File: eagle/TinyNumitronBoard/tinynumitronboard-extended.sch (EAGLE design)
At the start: 25 parts

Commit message: Extended version : schema is ok but board is beta.
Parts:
- added LED3, LED4: (no value), led:LEDKA-3528ASYC
- added R17, R18, R19, R20, R21, R22, R23, R24, R25, R26, R27, R28, R29, R30, R31, R32: (no value), resistor:R-EU_0207/10
- added U$5, U$7: IV16TINY_NUMITRON, kalshagar:IV16TINY_NUMITRON
- added U$6, U$8: 74HC595_SMDDIP_COMBOTHINPAD, kalshagar:74HC595_SMDDIP_COMBOTHINPAD
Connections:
- new net N$39: R17.2, U$5.BOTTOMLEFT
- new net N$40: R18.2, U$5.BOTTOM
- new net N$41: R19.2, U$5.MIDDLE
- new net N$42: R20.2, U$5.TOPLEFT
- new net N$43: R21.2, U$5.TOP
- new net N$44: R22.2, U$5.BOTTOMRIGHT
- new net N$45: R23.2, U$5.TOPRIGHT
- new net N$46: R17.1, U$6.QA
- new net N$47: R18.1, U$6.QB
- new net N$48: R19.1, U$6.QC
- new net N$49: R20.1, U$6.QD
- new net N$50: R21.1, U$6.QE
- new net N$51: R22.1, U$6.QF
- new net N$52: R23.1, U$6.QG
- new net N$53: R24.1, U$6.QH
- new net N$54: LED3.A, R24.2, U$5.DOT
- new net N$62: R25.2, U$7.BOTTOMLEFT
- new net N$63: R26.2, U$7.BOTTOM
- new net N$64: R27.2, U$7.MIDDLE
- new net N$65: R28.2, U$7.TOPLEFT
- new net N$66: R29.2, U$7.TOP
- new net N$67: R30.2, U$7.BOTTOMRIGHT
- new net N$68: R31.2, U$7.TOPRIGHT
- new net N$69: R25.1, U$8.QA
- new net N$70: R26.1, U$8.QB
- new net N$71: R27.1, U$8.QC
- new net N$72: R28.1, U$8.QD
- new net N$73: R29.1, U$8.QE
- new net N$74: R30.1, U$8.QF
- new net N$75: R31.1, U$8.QG
- new net N$76: R32.1, U$8.QH
- new net N$77: LED4.A, R32.2, U$7.DOT
- new net N$78: U$4.SER
- net GND: now also LED3.C, LED4.C, U$4.G, U$4.GND
- net N$18: now also U$4.RCK
- net N$19: now also U$4.SCK
- net N$22: now also U$4.QH*
- net VCC: now also U$4.SCL, U$4.VCC, U$5.VCC, U$7.VCC
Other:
- moved on the sheet: JP_OUTPUT, LED2, R10, R11, R12, R13, R14, R15, R16, R9, U$4

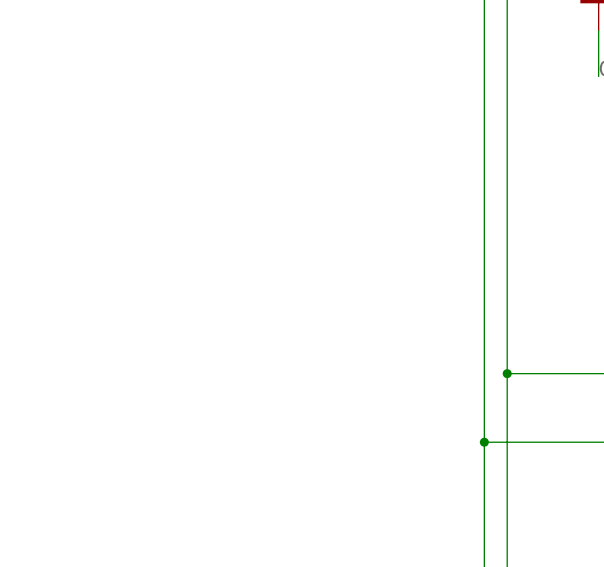
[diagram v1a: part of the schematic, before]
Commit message: added mounting holes and improved placement.
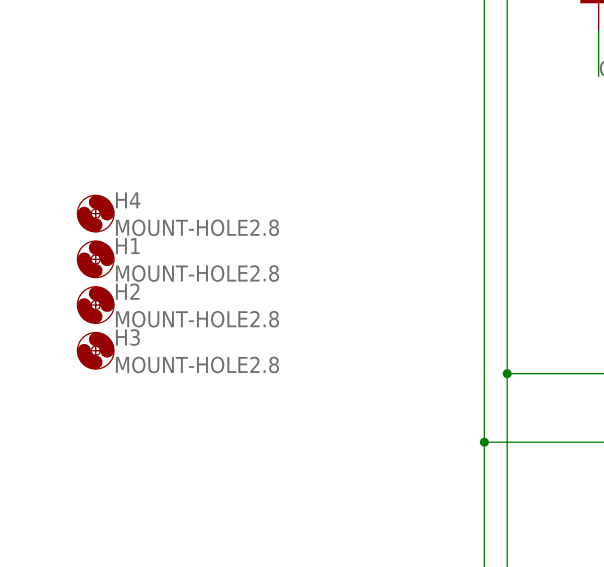
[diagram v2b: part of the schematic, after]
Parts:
- added H1, H2, H3, H4: MOUNT-HOLE2.8, holes:MOUNT-HOLE2.8
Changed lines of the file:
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@@
 <layer number="144" name="Drill_legend" color="7" fill="1" visible="no" active="yes"/>
 <layer number="151" name="HeatSink" color="7" fill="1" visible="no" active="yes"/>
+<layer number="199" name="Contour" color="7" fill="1" visible="yes" active="yes"/>
 <layer number="200" name="200bmp" color="1" fill="10" visible="no" active="yes"/>
 <layer number="201" name="201bmp" color="2" fill="10" visible="no" active="yes"/>
@@
 <part name="R32" library="resistor" deviceset="R-EU_" device="0207/10"/>
 <part name="U$8" library="kalshagar" deviceset="74HC595_SMDDIP_COMBO" device="THINPAD"/>
+<part name="H4" library="holes" deviceset="MOUNT-HOLE" device="2.8"/>
+<part name="H1" library="holes" deviceset="MOUNT-HOLE" device="2.8"/>
+<part name="H2" library="holes" deviceset="MOUNT-HOLE" device="2.8"/>
+<part name="H3" library="holes" deviceset="MOUNT-HOLE" device="2.8"/>
 </parts>
 <sheets>
@@
 <instance part="R32" gate="G$1" x="-17.78" y="-66.04"/>
 <instance part="U$8" gate="G$1" x="-48.26" y="-63.5"/>
+<instance part="H4" gate="G$1" x="-144.78" y="22.86"/>
+<instance part="H1" gate="G$1" x="-144.78" y="17.78"/>
+<instance part="H2" gate="G$1" x="-144.78" y="12.7"/>
+<instance part="H3" gate="G$1" x="-144.78" y="7.62"/>
 </instances>
 <busses>

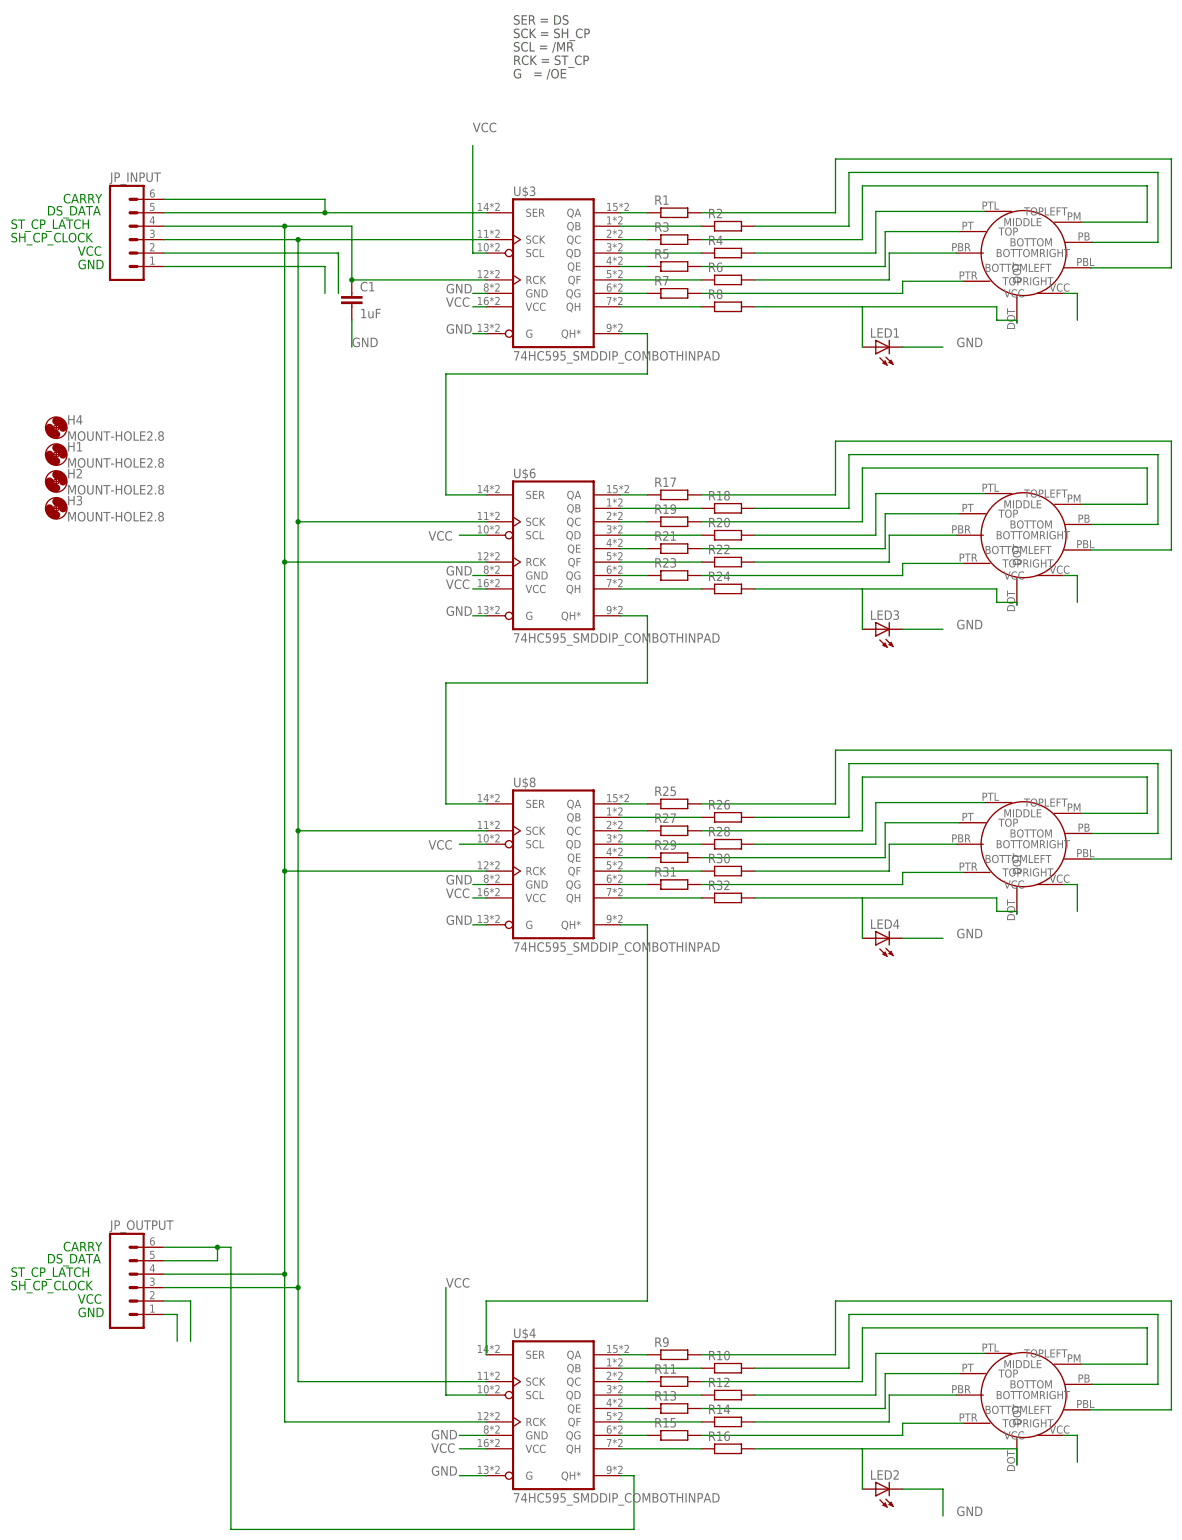
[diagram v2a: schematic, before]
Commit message: fixed the lots of missing wires ! all connections should be ok now.
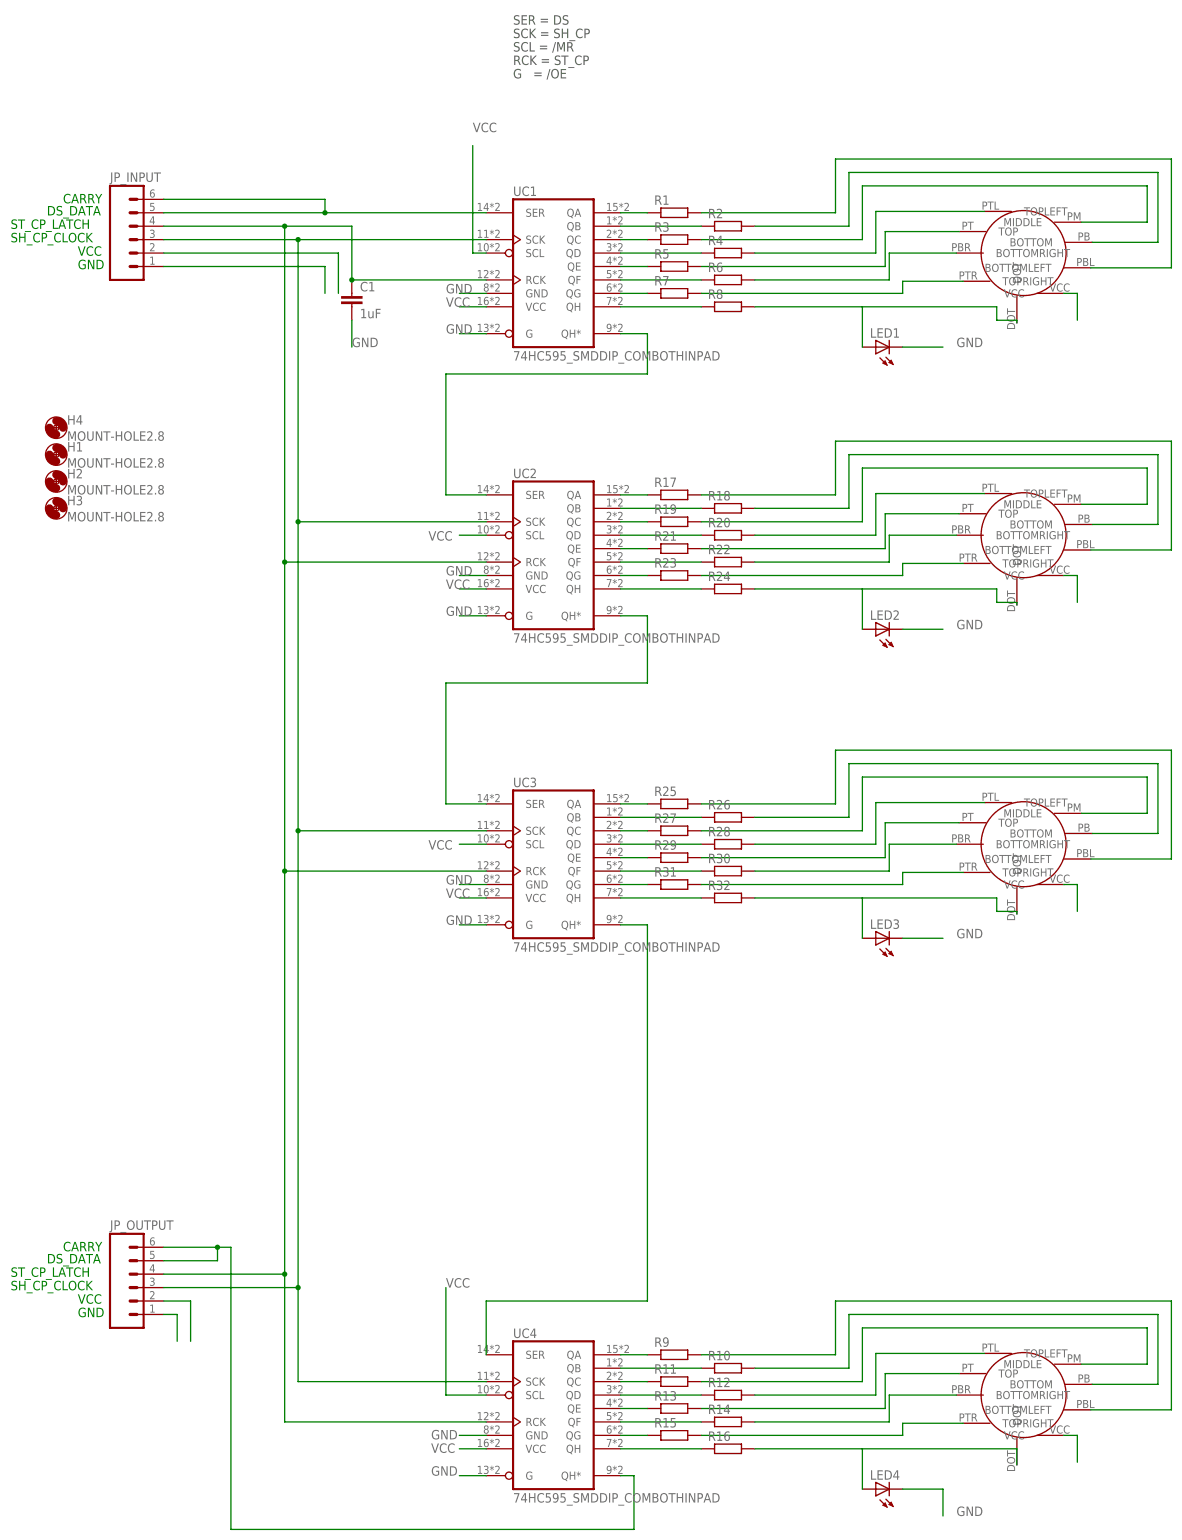
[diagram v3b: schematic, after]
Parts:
- renumbered U$3 to UC1, U$4 to UC4, U$6 to UC2, U$8 to UC3
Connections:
- removed net N$15: JP_INPUT.5, JP_INPUT.6
- removed net N$18: C1.1, JP_INPUT.4, JP_OUTPUT.4, UC4.RCK
- removed net N$19: JP_INPUT.3, JP_OUTPUT.3, UC4.SCK
- new net N$23: UC1.QH*, UC2.SER
- new net N$58: UC2.QH*, UC3.SER
- new net RCK: C1.1, JP_INPUT.4, JP_OUTPUT.4, UC1.RCK, UC2.RCK, UC3.RCK, UC4.RCK
- new net SCK: JP_INPUT.3, JP_OUTPUT.3, UC1.SCK, UC2.SCK, UC3.SCK, UC4.SCK
- new net SER: JP_INPUT.5, JP_INPUT.6, UC1.SER
- net GND: now also UC1.G, UC1.GND, UC2.G, UC2.GND, UC3.G, UC3.GND
- net N$37: now also LED4.A; no longer LED2.A
- net N$54: now also LED2.A; no longer LED3.A
- net N$77: now also LED3.A; no longer LED4.A
- net N$78: now also UC3.QH*
- net VCC: now also UC1.SCL, UC1.VCC, UC2.SCL, UC2.VCC, UC3.SCL, UC3.VCC
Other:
- moved on the sheet: LED2, LED3, LED4

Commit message: Version 1.0 sent to production with nice image on the top.
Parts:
- R1, R10, R11, R12, R13, R14, R15, R16, R17, R18, R19, R2, R20, R21, R22, R23, R24, R25, R26, R27, R28, R29, R3, R30, R31, R32, R4, R5, R6, R7, R8, R9: value (none) -> RESISTOR_COMBO1206; device resistor:R-EU_0207/10 -> kalshagar:RESISTOR_COMBO1206
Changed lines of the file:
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@@
 <parts>
 <part name="U$1" library="kalshagar" deviceset="IV16TINY_NUMITRON" device=""/>
-<part name="R1" library="resistor" deviceset="R-EU_" device="0207/10"/>
-<part name="R2" library="resistor" deviceset="R-EU_" device="0207/10"/>
-<part name="R3" library="resistor" deviceset="R-EU_" device="0207/10"/>
-<part name="R4" library="resistor" deviceset="R-EU_" device="0207/10"/>
-<part name="R5" library="resistor" deviceset="R-EU_" device="0207/10"/>
-<part name="R6" library="resistor" deviceset="R-EU_" device="0207/10"/>
-<part name="R7" library="resistor" deviceset="R-EU_" device="0207/10"/>
+<part name="R1" library="kalshagar" deviceset="RESISTOR_COMBO1206" device=""/>
+<part name="R2" library="kalshagar" deviceset="RESISTOR_COMBO1206" device=""/>
+<part name="R3" library="kalshagar" deviceset="RESISTOR_COMBO1206" device=""/>
+<part name="R4" library="kalshagar" deviceset="RESISTOR_COMBO1206" device=""/>
+<part name="R5" library="kalshagar" deviceset="RESISTOR_COMBO1206" device=""/>
+<part name="R6" library="kalshagar" deviceset="RESISTOR_COMBO1206" device=""/>
+<part name="R7" library="kalshagar" deviceset="RESISTOR_COMBO1206" device=""/>
 <part name="JP_INPUT" library="SparkFun" deviceset="M06" device="SIP"/>
 <part name="LED1" library="led" deviceset="LED" device="KA-3528ASYC"/>
-<part name="R8" library="resistor" deviceset="R-EU_" device="0207/10"/>
+<part name="R8" library="kalshagar" deviceset="RESISTOR_COMBO1206" device=""/>
 <part name="C1" library="resistor" deviceset="C-EU" device="050-024X044" value="1uF"/>
 <part name="JP_OUTPUT" library="SparkFun" deviceset="M06" device="SIP"/>
 <part name="U$2" library="kalshagar" deviceset="IV16TINY_NUMITRON" device=""/>
-<part name="R9" library="resistor" deviceset="R-EU_" device="0207/10"/>
-<part name="R10" library="resistor" deviceset="R-EU_" device="0207/10"/>
-<part name="R11" library="resistor" deviceset="R-EU_" device="0207/10"/>
-<part name="R12" library="resistor" deviceset="R-EU_" device="0207/10"/>
-<part name="R13" library="resistor" deviceset="R-EU_" device="0207/10"/>
-<part name="R14" library="resistor" deviceset="R-EU_" device="0207/10"/>
-<part name="R15" library="resistor" deviceset="R-EU_" device="0207/10"/>
+<part name="R9" library="kalshagar" deviceset="RESISTOR_COMBO1206" device=""/>
+<part name="R10" library="kalshagar" deviceset="RESISTOR_COMBO1206" device=""/>
+<part name="R11" library="kalshagar" deviceset="RESISTOR_COMBO1206" device=""/>
+<part name="R12" library="kalshagar" deviceset="RESISTOR_COMBO1206" device=""/>
+<part name="R13" library="kalshagar" deviceset="RESISTOR_COMBO1206" device=""/>
+<part name="R14" library="kalshagar" deviceset="RESISTOR_COMBO1206" device=""/>
+<part name="R15" library="kalshagar" deviceset="RESISTOR_COMBO1206" device=""/>
 <part name="LED4" library="led" deviceset="LED" device="KA-3528ASYC"/>
-<part name="R16" library="resistor" deviceset="R-EU_" device="0207/10"/>
+<part name="R16" library="kalshagar" deviceset="RESISTOR_COMBO1206" device=""/>
 <part name="UC1" library="kalshagar" deviceset="74HC595_SMDDIP_COMBO" device="THINPAD"/>
 <part name="UC4" library="kalshagar" deviceset="74HC595_SMDDIP_COMBO" device="THINPAD"/>
 <part name="U$5" library="kalshagar" deviceset="IV16TINY_NUMITRON" device=""/>
-<part name="R17" library="resistor" deviceset="R-EU_" device="0207/10"/>
-<part name="R18" library="resistor" deviceset="R-EU_" device="0207/10"/>
-<part name="R19" library="resistor" deviceset="R-EU_" device="0207/10"/>
-<part name="R20" library="resistor" deviceset="R-EU_" device="0207/10"/>
-<part name="R21" library="resistor" deviceset="R-EU_" device="0207/10"/>
-<part name="R22" library="resistor" deviceset="R-EU_" device="0207/10"/>
-<part name="R23" library="resistor" deviceset="R-EU_" device="0207/10"/>
+<part name="R17" library="kalshagar" deviceset="RESISTOR_COMBO1206" device=""/>
+<part name="R18" library="kalshagar" deviceset="RESISTOR_COMBO1206" device=""/>
+<part name="R19" library="kalshagar" deviceset="RESISTOR_COMBO1206" device=""/>
+<part name="R20" library="kalshagar" deviceset="RESISTOR_COMBO1206" device=""/>
+<part name="R21" library="kalshagar" deviceset="RESISTOR_COMBO1206" device=""/>
+<part name="R22" library="kalshagar" deviceset="RESISTOR_COMBO1206" device=""/>
+<part name="R23" library="kalshagar" deviceset="RESISTOR_COMBO1206" device=""/>
 <part name="LED2" library="led" deviceset="LED" device="KA-3528ASYC"/>
-<part name="R24" library="resistor" deviceset="R-EU_" device="0207/10"/>
+<part name="R24" library="kalshagar" deviceset="RESISTOR_COMBO1206" device=""/>
 <part name="UC2" library="kalshagar" deviceset="74HC595_SMDDIP_COMBO" device="THINPAD"/>
 <part name="U$7" library="kalshagar" deviceset="IV16TINY_NUMITRON" device=""/>
-<part name="R25" library="resistor" deviceset="R-EU_" device="0207/10"/>
-<part name="R26" library="resistor" deviceset="R-EU_" device="0207/10"/>
-<part name="R27" library="resistor" deviceset="R-EU_" device="0207/10"/>
-<part name="R28" library="resistor" deviceset="R-EU_" device="0207/10"/>
-<part name="R29" library="resistor" deviceset="R-EU_" device="0207/10"/>
-<part name="R30" library="resistor" deviceset="R-EU_" device="0207/10"/>
-<part name="R31" library="resistor" deviceset="R-EU_" device="0207/10"/>
+<part name="R25" library="kalshagar" deviceset="RESISTOR_COMBO1206" device=""/>
+<part name="R26" library="kalshagar" deviceset="RESISTOR_COMBO1206" device=""/>
+<part name="R27" library="kalshagar" deviceset="RESISTOR_COMBO1206" device=""/>
+<part name="R28" library="kalshagar" deviceset="RESISTOR_COMBO1206" device=""/>
+<part name="R29" library="kalshagar" deviceset="RESISTOR_COMBO1206" device=""/>
+<part name="R30" library="kalshagar" deviceset="RESISTOR_COMBO1206" device=""/>
+<part name="R31" library="kalshagar" deviceset="RESISTOR_COMBO1206" device=""/>
 <part name="LED3" library="led" deviceset="LED" device="KA-3528ASYC"/>
-<part name="R32" library="resistor" deviceset="R-EU_" device="0207/10"/>
+<part name="R32" library="kalshagar" deviceset="RESISTOR_COMBO1206" device=""/>
 <part name="UC3" library="kalshagar" deviceset="74HC595_SMDDIP_COMBO" device="THINPAD"/>
 <part name="H4" library="holes" deviceset="MOUNT-HOLE" device="2.8"/>
